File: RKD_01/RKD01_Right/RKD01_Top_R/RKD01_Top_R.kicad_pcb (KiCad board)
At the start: 2 copper layers, 209.6 x 126.2 mm, 50 parts, among them M1 Mark, M2 Mark, M3 Mark, M4 Mark, M5 Mark, SW36 SW_Push, SW37 SW_Push, SW38 SW_Push, SW39 SW_Push, SW40 SW_Push, SW41 SW_Push, SW42 SW_Push, SW43 SW_Push, SW44 SW_Push, SW45 SW_Push, SW46 SW_Push, SW47 SW_Push, SW48 SW_Push, SW49 SW_Push, SW50 SW_Push, SW51 SW_Push, SW52 SW_Push, SW53 SW_Push, SW54 SW_Push, SW55 SW_Push, SW56 SW_Push, SW57 SW_Push, SW58 SW_Push, SW59 SW_Push, SW60 SW_Push, SW61 SW_Push, SW62 SW_Push, SW63 SW_Push, SW64 SW_Push, SW65 SW_Push, SW66 SW_PUSH, SW66 SW_Push, SW67 SW_Push, SW68 SW_Push, SW69 SW_Push, SW70 SW_Push, SW71 SW_Push, SW72 SW_Push, SW73 SW_Push, SW74 SW_Push, SW75 SW_Push, SW76 SW_Push, SW77 SW_Push, SW78 SW_Push

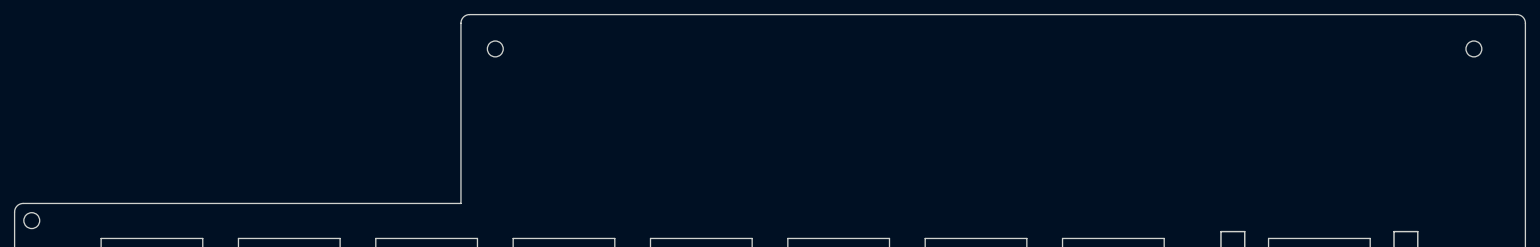
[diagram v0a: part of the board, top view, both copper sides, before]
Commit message: promicro部分拡張
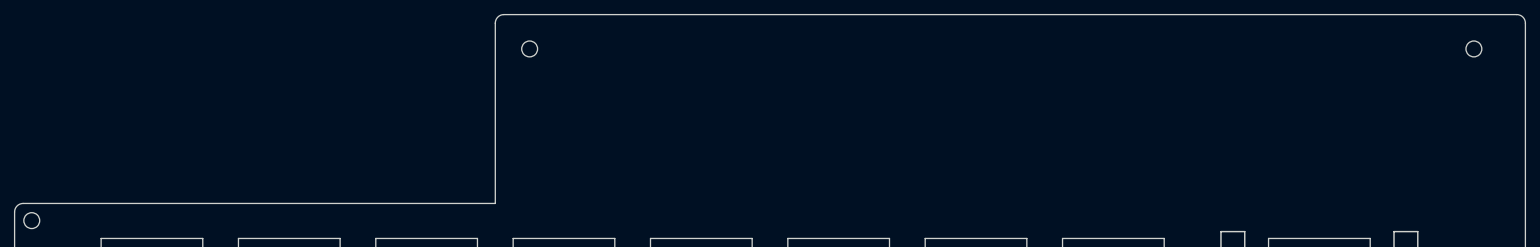
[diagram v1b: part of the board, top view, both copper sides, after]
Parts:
- moved M1 4.76 mm to (92.9, 23.8)
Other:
- outline, holes or cut-outs redrawn
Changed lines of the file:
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@@
 	(footprint "kbd_Hole:m2_Screw_Hole"
 		(layer "F.Cu")
-		(at 88.1063 23.8125)
+		(at 92.86875 23.8125)
 		(descr "Mounting Hole 2.2mm, no annular, M2")
 		(tags "mounting hole 2.2mm no annular m2")
@@
 	)
 	(gr_arc
-		(start 83.343775 20.24065)
-		(mid 83.692468 19.398768)
-		(end 84.53435 19.050075)
+		(start 88.10635 20.240675)
+		(mid 88.455047 19.398797)
+		(end 89.296925 19.0501)
 		(stroke
 			(width 0.05)
@@
 	)
 	(gr_line
-		(start 83.343775 20.24065)
-		(end 83.34375 45.24375)
+		(start 88.10625 20.24065)
+		(end 88.106225 45.24375)
 		(stroke
 			(width 0.05)
@@
 	(gr_line
 		(start 229.790625 19.05)
-		(end 84.53435 19.050075)
+		(end 89.296875 19.050075)
 		(stroke
 			(width 0.05)
@@
 	)
 	(gr_line
-		(start 83.34375 45.24375)
+		(start 88.10625 45.24375)
 		(end 22.62185 45.243725)
 		(stroke

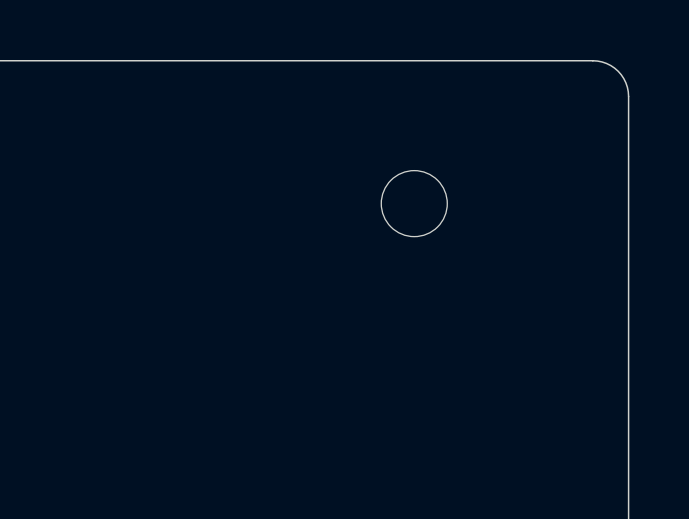
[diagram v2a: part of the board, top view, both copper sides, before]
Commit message: ネジ穴位置の誤り修正
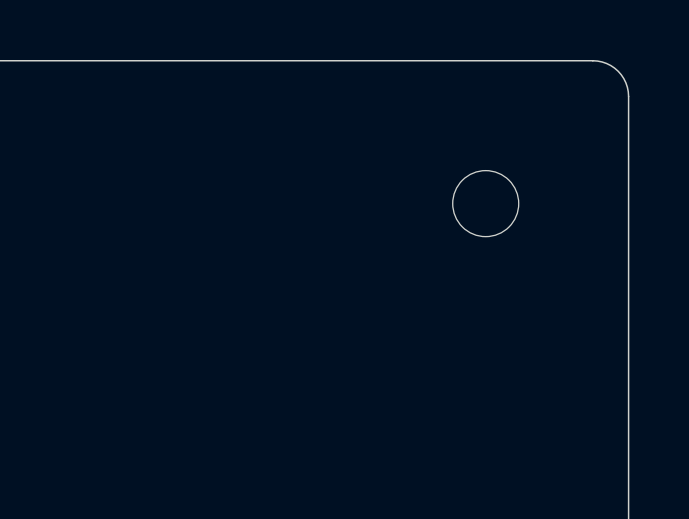
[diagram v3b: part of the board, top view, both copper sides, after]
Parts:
- moved M2 2.38 mm to (226.2, 23.8)
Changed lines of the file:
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@@
 	(footprint "kbd_Hole:m2_Screw_Hole"
 		(layer "F.Cu")
-		(at 223.8375 23.8125)
+		(at 226.21875 23.8125)
 		(descr "Mounting Hole 2.2mm, no annular, M2")
 		(tags "mounting hole 2.2mm no annular m2")

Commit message: 配置変更
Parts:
- added M7: Mark, kbd_Hole:m2_Screw_Hole, F.Cu at (164.3, 66.7)
- added M8: Mark, kbd_Hole:m2_Screw_Hole, F.Cu at (83.3, 104.8)
- added SW75: SW_Push, kbd_SW_Hole:SW_Hole_1u, F.Cu at (135.7, 133.3)
- SW55: renamed from SW40; footprint kbd_SW_Hole:SW_Hole_1u -> kbd_SW_Hole:SW_Hole_1.25u
- SW60: renamed from SW45; footprint kbd_SW_Hole:SW_Hole_1.5u -> kbd_SW_Hole:SW_Hole_1.25u
- SW70: renamed from SW55; footprint kbd_SW_Hole:SW_Hole_1.25u -> kbd_SW_Hole:SW_Hole_1u
- SW80: renamed from SW64; footprint kbd_SW_Hole:SW_Hole_1.25u -> kbd_SW_Hole:SW_Hole_1u
- SW92: renamed from SW76; footprint kbd_SW_Hole:SW_Hole_1u -> kbd_SW_Hole:SW_Hole_1.5u
- moved SW70 11.9 mm to (116.7, 133.3)
- moved SW65 9.53 mm to (90.5, 133.3)
- moved SW55 7.14 mm to (38.1, 133.3)
- moved SW60 7.14 mm to (61.9, 133.3)
- moved SW80 2.38 mm to (154.8, 133.3)
- renumbered SW36 to SW51, SW37 to SW52, SW38 to SW53, SW39 to SW54, SW41 to SW56, SW42 to SW57, SW43 to SW58, SW44 to SW59, SW46 to SW61, SW47 to SW62, SW48 to SW63, SW49 to SW64, SW50 to SW65, SW51 to SW66, SW52 to SW67, SW53 to SW68, SW54 to SW69, SW56 to SW71, SW57 to SW72, SW58 to SW73, SW59 to SW74, SW60 to SW76, SW61 to SW77, SW62 to SW78, SW63 to SW79, SW65 to SW81, SW66 to SW82, SW67 to SW83, SW68 to SW84, SW69 to SW85, SW70 to SW86, SW71 to SW87, SW72 to SW88, SW73 to SW89, SW74 to SW90, SW75 to SW91, SW77 to SW94, SW78 to SW95
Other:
- board size 209.6 x 126.2 mm -> 209.5 x 126.2 mm
- board text added: "RKD01_Right v1.5"
- board text removed: "RKD01_Right v1.0"

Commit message: バージョン表記を修正
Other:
- board text added: "RKD01_Right v2"
- board text removed: "RKD01_Right v1.5"
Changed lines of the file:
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@@
 		(layer "F.Fab")
 	)
-	(gr_text "RKD01_Right v1.5"
+	(gr_text "RKD01_Right v2"
 		(at 214.3125 23.8125 0)
 		(layer "B.SilkS")

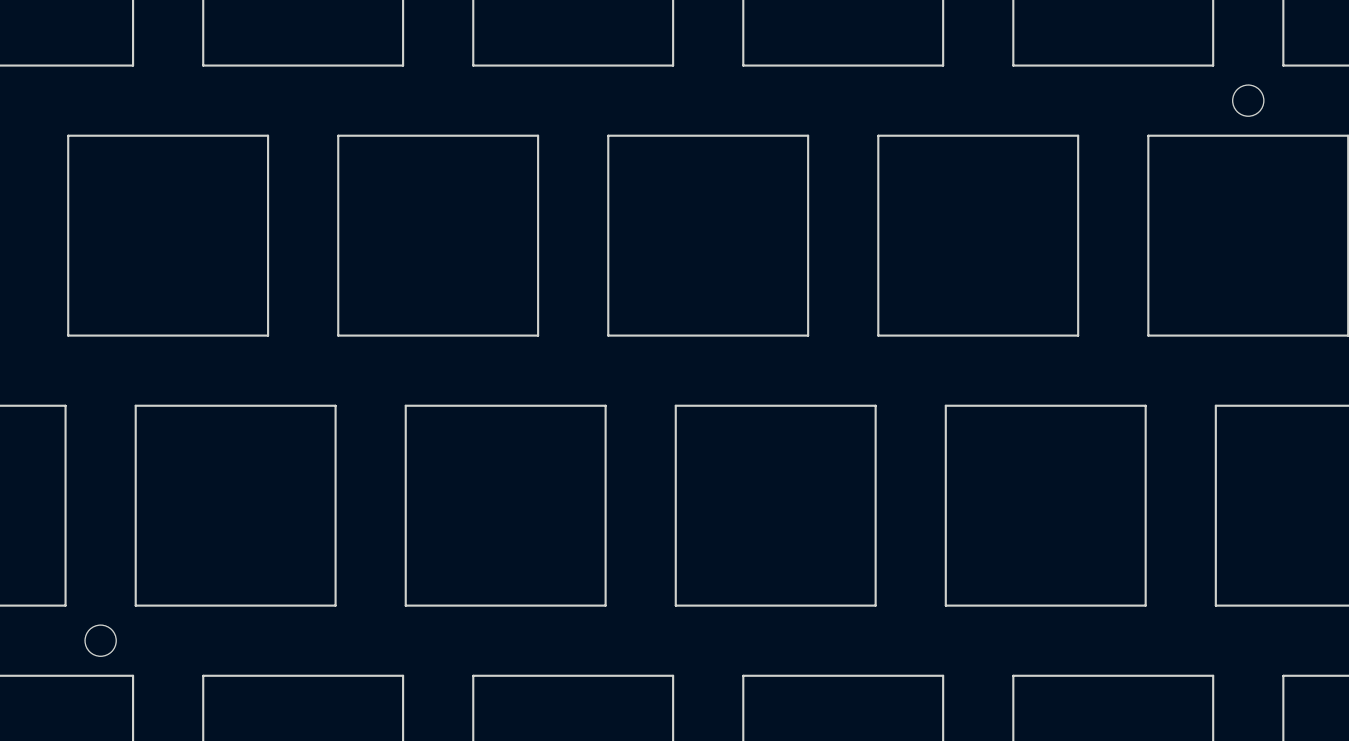
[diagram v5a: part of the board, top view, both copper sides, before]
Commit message: スイッチフットプリントをChocV2に修正
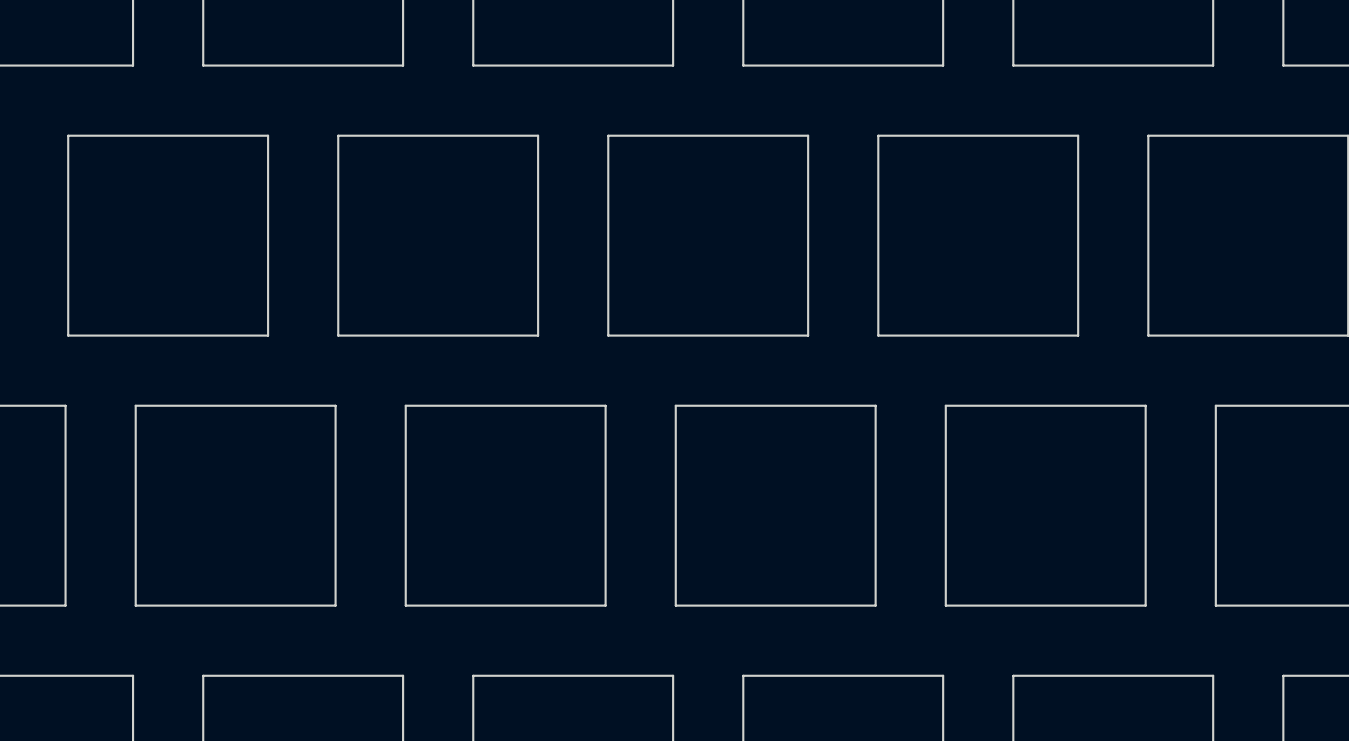
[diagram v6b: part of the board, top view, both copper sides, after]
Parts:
- removed M7, M8: Mark, kbd_Hole:m2_Screw_Hole
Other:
- board text added: "RKD01_Right v1.5"
- board text removed: "RKD01_Right v2"
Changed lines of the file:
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@@
 		)
 	)
-	(footprint "kbd_Hole:m2_Screw_Hole"
-		(layer "F.Cu")
-		(at 164.3063 66.675)
-		(descr "Mounting Hole 2.2mm, no annular, M2")
-		(tags "mounting hole 2.2mm no annular m2")
-		(property "Reference" "M7"
-			(at 0 -3.2 0)
-			(layer "F.Fab")
-			(effects
-				(font
-					(size 1 1)
-					(thickness 0.15)
-				)
-			)
-		)
-		(property "Value" "Mark"
-			(at 0 3.2 0)
-			(layer "F.Fab")
-			(effects
-				(font
-					(size 1 1)
-					(thickness 0.15)
-				)
-			)
-		)
-		(property "Footprint" "kbd_Hole:m2_Screw_Hole"
-			(at 0 0 0)
-			(layer "F.Fab")
-			(hide yes)
-			(effects
-				(font
-					(size 1.27 1.27)
-					(thickness 0.15)
-				)
-			)
-		)
-		(property "Datasheet" ""
-			(at 0 0 0)
-			(layer "F.Fab")
-			(hide yes)
-			(effects
-				(font
-					(size 1.27 1.27)
-					(thickness 0.15)
-				)
-			)
-		)
-		(property "Description" ""
-			(at 0 0 0)
-			(layer "F.Fab")
-			(hide yes)
-			(effects
-				(font
-					(size 1.27 1.27)
-					(thickness 0.15)
-				)
-			)
-		)
-		(sheetname "ルート")
-		(sheetfile "RKD01_Assemble_R.kicad_sch")
-		(attr exclude_from_pos_files exclude_from_bom)
-		(fp_circle
-			(center 0 0)
-			(end 2.2 0)
-			(stroke
-				(width 0.15)
-				(type solid)
-			)
-			(fill none)
-			(layer "Cmts.User")
-		)
-		(fp_circle
-			(center 0 0)
-			(end 2.45 0)
-			(stroke
-				(width 0.05)
-				(type solid)
-			)
-			(fill none)
-			(layer "F.CrtYd")
-		)
-		(fp_text user "${REFERENCE}"
-			(at 0.3 0 0)
-			(layer "F.Fab")
-			(effects
-				(font
-					(size 1 1)
-					(thickness 0.15)
-				)
-			)
-		)
-		(pad "" np_thru_hole circle
-			(at 0 0)
-			(size 2.2 2.2)
-			(drill 2.2)
-			(layers "*.Cu" "*.Mask")
-		)
-	)
 	(footprint "kbd_SW_Hole:SW_Hole_1u"
 		(layer "F.Cu")
@@
 		)
 	)
-	(footprint "kbd_Hole:m2_Screw_Hole"
-		(layer "F.Cu")
-		(at 83.3438 104.775)
-		(descr "Mounting Hole 2.2mm, no annular, M2")
-		(tags "mounting hole 2.2mm no annular m2")
-		(property "Reference" "M8"
-			(at 0 -3.2 0)
-			(layer "F.Fab")
-			(effects
-				(font
-					(size 1 1)
-					(thickness 0.15)
-				)
-			)
-		)
-		(property "Value" "Mark"
-			(at 0 3.2 0)
-			(layer "F.Fab")
-			(effects
-				(font
-					(size 1 1)
-					(thickness 0.15)
-				)
-			)
-		)
-		(property "Footprint" "kbd_Hole:m2_Screw_Hole"
-			(at 0 0 0)
-			(layer "F.Fab")
-			(hide yes)
-			(effects
-				(font
-					(size 1.27 1.27)
-					(thickness 0.15)
-				)
-			)
-		)
-		(property "Datasheet" ""
-			(at 0 0 0)
-			(layer "F.Fab")
-			(hide yes)
-			(effects
-				(font
-					(size 1.27 1.27)
-					(thickness 0.15)
-				)
-			)
-		)
-		(property "Description" ""
-			(at 0 0 0)
-			(layer "F.Fab")
-			(hide yes)
-			(effects
-				(font
-					(size 1.27 1.27)
-					(thickness 0.15)
-				)
-			)
-		)
-		(sheetname "ルート")
-		(sheetfile "RKD01_Assemble_R.kicad_sch")
-		(attr exclude_from_pos_files exclude_from_bom)
-		(fp_circle
-			(center 0 0)
-			(end 2.2 0)
-			(stroke
-				(width 0.15)
-				(type solid)
-			)
-			(fill none)
-			(layer "Cmts.User")
-		)
-		(fp_circle
-			(center 0 0)
-			(end 2.45 0)
-			(stroke
-				(width 0.05)
-				(type solid)
-			)
-			(fill none)
-			(layer "F.CrtYd")
-		)
-		(fp_text user "${REFERENCE}"
-			(at 0.3 0 0)
-			(layer "F.Fab")
-			(effects
-				(font
-					(size 1 1)
-					(thickness 0.15)
-				)
-			)
-		)
-		(pad "" np_thru_hole circle
-			(at 0 0)
-			(size 2.2 2.2)
-			(drill 2.2)
-			(layers "*.Cu" "*.Mask")
-		)
-	)
 	(footprint "kbd_SW_Hole:SW_Hole_1u"
 		(layer "F.Cu")
@@
 		(layer "F.Fab")
 	)
-	(gr_text "RKD01_Right v2"
+	(gr_text "RKD01_Right v1.5"
 		(at 214.3125 23.8125 0)
 		(layer "B.SilkS")
